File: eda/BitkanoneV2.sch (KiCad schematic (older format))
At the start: 33 parts, among them J202 5VUSB, J211 JH23, J212 JL23, J231 Jumper, J232 Jumper, J233 Jumper, J234 Jumper, Q501 PH_NPN, Q502 PH_NPN, U201 BluePill_STM32F103C, U202 MCP2551-I-SN, U301 6DOF, X101 01x02M, X102 01x02M, X200 01x03M, X201 5VUSB, X231 Bus, X232 Bus, X233 Bus, X234 Bus, X401 MotorCon, X42 Conn_01x07_Male, X990 Conn_01x01, X991 Conn_01x01

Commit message: USB port added; Mounting holes added; Silk screen measurements added
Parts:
- added H1, H2, H3: MountingHole_Pad, MountingHole:MountingHole_3.2mm_M3_Pad_Via, symbol Mechanical:MountingHole_Pad
- added JU1, JU2: Jumper, Jumper:SolderJumper-2_P1.3mm_Open_RoundedPad1.0x1.5mm, symbol Jumper:SolderJumper_2_Open
- added XU1: USB_B_Micro, Connector_USB:USB_Micro-B_Molex-105017-0001, symbol Connector:USB_B_Micro
- added bitkanoneV2: GNU Logo, Symbol:Symbol_GNU-Logo_SilkscreenTop, symbol Mechanical:MountingHole
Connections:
- net +5V: now also XU1.1 (VBUS)
- net GND: now also H1.1, H2.1, H3.1, XU1.4 (ID), XU1.5 (GND), XU1.6 (Shield)
- net USBD-: now reaches U201.28 (PA11_USB_D-)
- net USBD-: now also JU2.2 (B)
- net USBD+: now reaches U201.29 (PA12_USBD+)
- net USBD+: now also JU1.2 (B)
- new net: JU2.1 (A), XU1.2 (D-)
- new net: JU1.1 (A), XU1.3 (D+)
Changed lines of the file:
@@
 Text Label 5750 4400 0    50   ~ 0
 RX1
+$Comp
+L power:GND #PWR01
+U 1 1 5C11C39D
+P 10000 5800
+F 0 "#PWR01" H 10000 5550 50  0001 C CNN
+F 1 "GND" H 10005 5627 50  0000 C CNN
+F 2 "" H 10000 5800 50  0001 C CNN
+F 3 "" H 10000 5800 50  0001 C CNN
+	1    10000 5800
+	1    0    0    -1
+$EndComp
+$Comp
+L Mechanical:MountingHole_Pad H3
+U 1 1 5C11C4BF
+P 10200 5700
+F 0 "H3" V 10154 5850 50  0000 L CNN
+F 1 "MountingHole_Pad" V 10245 5850 50  0000 L CNN
+F 2 "MountingHole:MountingHole_3.2mm_M3_Pad_Via" H 10200 5700 50  0001 C CNN
+F 3 "~" H 10200 5700 50  0001 C CNN
+	1    10200 5700
+	0    1    1    0
+$EndComp
+$Comp
+L Mechanical:MountingHole_Pad H1
+U 1 1 5C14261A
+P 10200 5300
+F 0 "H1" V 10154 5450 50  0000 L CNN
+F 1 "MountingHole_Pad" V 10245 5450 50  0000 L CNN
+F 2 "MountingHole:MountingHole_3.2mm_M3_Pad_Via" H 10200 5300 50  0001 C CNN
+F 3 "~" H 10200 5300 50  0001 C CNN
+	1    10200 5300
+	0    1    1    0
+$EndComp
+$Comp
+L Mechanical:MountingHole_Pad H2
+U 1 1 5C142621
+P 10200 5500
+F 0 "H2" V 10154 5650 50  0000 L CNN
+F 1 "MountingHole_Pad" V 10245 5650 50  0000 L CNN
+F 2 "MountingHole:MountingHole_3.2mm_M3_Pad_Via" H 10200 5500 50  0001 C CNN
+F 3 "~" H 10200 5500 50  0001 C CNN
+	1    10200 5500
+	0    1    1    0
+$EndComp
+Wire Wire Line
+	10100 5300 10000 5300
+Wire Wire Line
+	10000 5300 10000 5500
+Wire Wire Line
+	10100 5500 10000 5500
+Connection ~ 10000 5500
+Wire Wire Line
+	10000 5500 10000 5700
+Wire Wire Line
+	10100 5700 10000 5700
+$Comp
+L Mechanical:MountingHole bitkanoneV2
+U 1 1 5C19C29E
+P 10250 5000
+F 0 "bitkanoneV2" H 10350 5046 50  0000 L CNN
+F 1 "GNU Logo" H 10350 4955 50  0000 L CNN
+F 2 "Symbol:Symbol_GNU-Logo_SilkscreenTop" H 10250 5000 50  0001 C CNN
+F 3 "~" H 10250 5000 50  0001 C CNN
+	1    10250 5000
+	1    0    0    -1
+$EndComp
+$Comp
+L Connector:USB_B_Micro XU1
+U 1 1 5C19D2E1
+P 2900 5650
+F 0 "XU1" H 2955 6117 50  0000 C CNN
+F 1 "USB_B_Micro" H 2955 6026 50  0000 C CNN
+F 2 "Connector_USB:USB_Micro-B_Molex-105017-0001" H 3050 5600 50  0001 C CNN
+F 3 "~" H 3050 5600 50  0001 C CNN
+	1    2900 5650
+	1    0    0    -1
+$EndComp
+$Comp
+L power:GND #PWR0133
+U 1 1 5C19D6F1
+P 3300 6250
+F 0 "#PWR0133" H 3300 6000 50  0001 C CNN
+F 1 "GND" H 3305 6077 50  0000 C CNN
+F 2 "" H 3300 6250 50  0001 C CNN
+F 3 "" H 3300 6250 50  0001 C CNN
+	1    3300 6250
+	1    0    0    -1
+$EndComp
+$Comp
+L power:+5V #PWR0134
+U 1 1 5C19D78F
+P 3300 5350
+F 0 "#PWR0134" H 3300 5200 50  0001 C CNN
+F 1 "+5V" H 3315 5478 50  0000 L CNN
+F 2 "" H 3300 5350 50  0001 C CNN
+F 3 "" H 3300 5350 50  0001 C CNN
+	1    3300 5350
+	1    0    0    -1
+$EndComp
+Wire Wire Line
+	2800 6050 2800 6150
+Wire Wire Line
+	2800 6150 2900 6150
+Wire Wire Line
+	2900 6150 2900 6050
+Wire Wire Line
+	2900 6150 3300 6150
+Wire Wire Line
+	3300 6150 3300 6250
+Connection ~ 2900 6150
+Wire Wire Line
+	3200 5850 3300 5850
+Wire Wire Line
+	3300 5850 3300 6150
+Connection ~ 3300 6150
+Wire Wire Line
+	3200 5450 3300 5450
+Text Label 5750 4200 0    50   ~ 0
+USBD+
+Text Label 5750 4300 0    50   ~ 0
+USBD-
+Text Label 3750 5650 0    50   ~ 0
+USBD+
+Text Label 3750 5750 0    50   ~ 0
+USBD-
+Wire Wire Line
+	5600 4200 5750 4200
+Wire Wire Line
+	5600 4300 5750 4300
+Wire Wire Line
+	3200 5650 3350 5650
+Wire Wire Line
+	3200 5750 3350 5750
+Wire Wire Line
+	10000 5800 10000 5700
+Connection ~ 10000 5700
+Wire Wire Line
+	3300 5450 3300 5350
+$Comp
+L Jumper:SolderJumper_2_Open JU1
+U 1 1 5C2FAC8C
+P 3500 5650
+F 0 "JU1" H 3500 5855 50  0000 C CNN
+F 1 "Jumper" H 3500 5764 50  0000 C CNN
+F 2 "Jumper:SolderJumper-2_P1.3mm_Open_RoundedPad1.0x1.5mm" H 3500 5650 50  0001 C CNN
+F 3 "~" H 3500 5650 50  0001 C CNN
+	1    3500 5650
+	1    0    0    -1
+$EndComp
+$Comp
+L Jumper:SolderJumper_2_Open JU2
+U 1 1 5C30698D
+P 3500 5750
+F 0 "JU2" H 3500 5550 50  0000 C CNN
+F 1 "Jumper" H 3500 5650 50  0000 C CNN
+F 2 "Jumper:SolderJumper-2_P1.3mm_Open_RoundedPad1.0x1.5mm" H 3500 5750 50  0001 C CNN
+F 3 "~" H 3500 5750 50  0001 C CNN
+	1    3500 5750
+	1    0    0    -1
+$EndComp
+Wire Wire Line
+	3650 5650 3750 5650
+Wire Wire Line
+	3650 5750 3750 5750
 $EndSCHEMATC

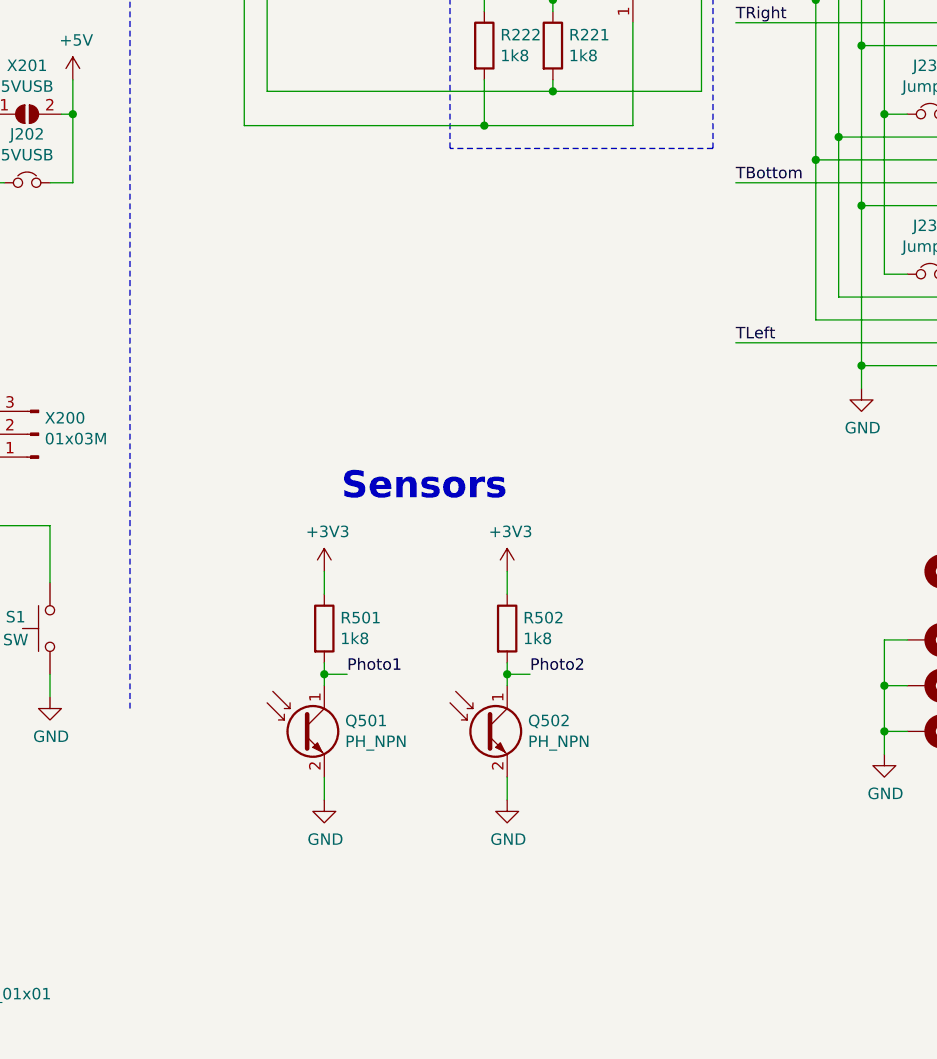
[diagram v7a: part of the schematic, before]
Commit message: Ledcom added to topo pins
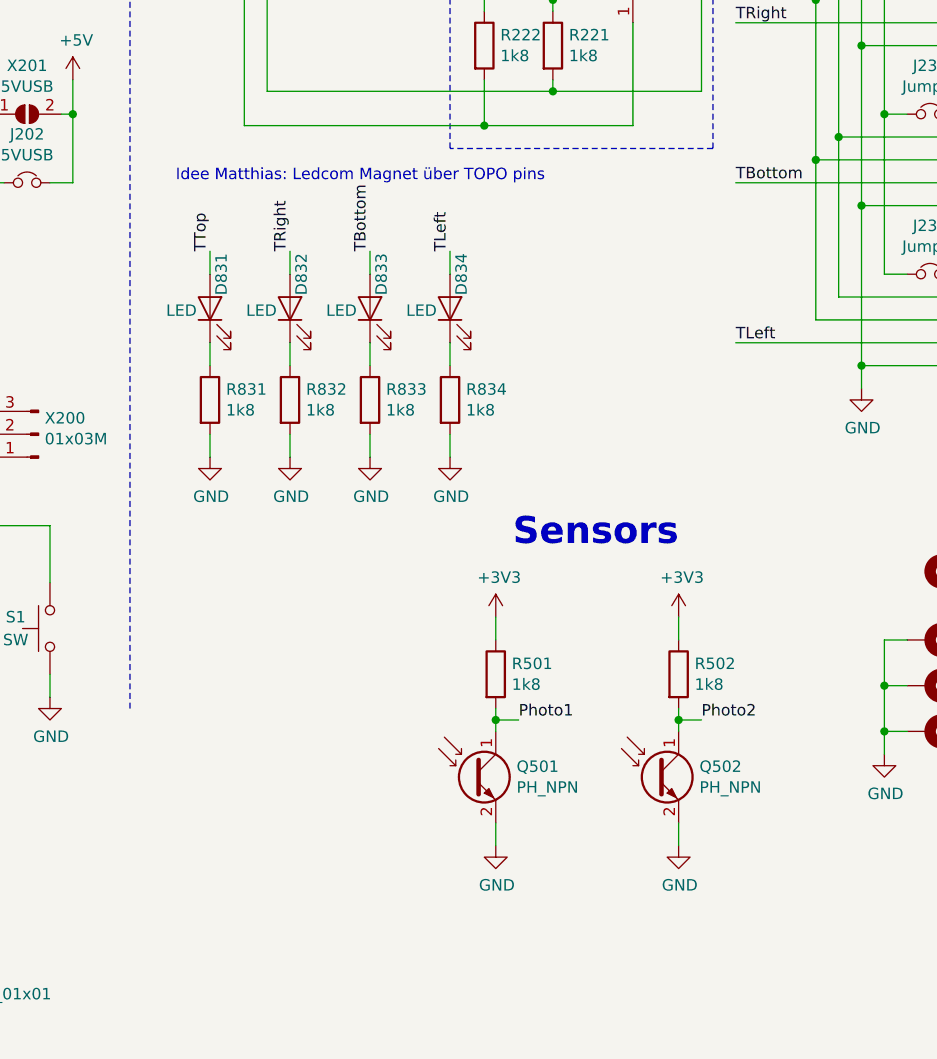
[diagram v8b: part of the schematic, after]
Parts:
- added D831, D832, D833, D834: LED, symbol Device:LED
- added R831, R832, R833, R834: 1k8, symbol Device:R
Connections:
- net GND: now also R831.2, R832.2, R833.2, R834.2
- net TBottom: now also D833.2 (A)
- net TLeft: now also D834.2 (A)
- net TRight: now also D832.2 (A)
- net TTop: now also D831.2 (A)
- new net: D831.1 (K), R831.1
- new net: D832.1 (K), R832.1
- new net: D833.1 (K), R833.1
- new net: D834.1 (K), R834.1
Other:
- note added: "Idee Matthias: Ledcom Magnet über TOPO pins"
- moved on the sheet: Q501, Q502, R501, R502
